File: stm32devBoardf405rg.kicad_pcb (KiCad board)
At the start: 4 copper layers, 0 parts

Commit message: assigned rough layout in pcb
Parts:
- added C1: 2u2, Capacitor_SMD:C_0603_1608Metric, F.Cu at (104.1, 142.2)
- added C10: 10n, Capacitor_SMD:C_0402_1005Metric, F.Cu at (165.6, 71.1)
- added C11: 12pF, Capacitor_SMD:C_0402_1005Metric, F.Cu at (68.1, 142.8)
- added C12: 12pF, Capacitor_SMD:C_0402_1005Metric, F.Cu at (68.1, 144.8)
- added C13: 47u, Capacitor_SMD:C_0603_1608Metric, F.Cu at (166.9, 129.5)
- added C14: 47u, Capacitor_SMD:C_0603_1608Metric, F.Cu at (164.3, 116.8)
- added C15: 47u, Capacitor_SMD:C_0603_1608Metric, F.Cu at (178.0, 114.2)
- added C16: 47u, Capacitor_SMD:C_0603_1608Metric, F.Cu at (178.0, 116.8)
- added C2: 2u2, Capacitor_SMD:C_0603_1608Metric, F.Cu at (104.1, 144.8)
- added C3: 4u7, Capacitor_SMD:C_0603_1608Metric, F.Cu at (98.3, 91.4)
- added C4: 100n, Capacitor_SMD:C_0402_1005Metric, F.Cu at (93.5, 87.5)
- added C5: 100n, Capacitor_SMD:C_0402_1005Metric, F.Cu at (93.5, 89.5)
- added C6: 100n, Capacitor_SMD:C_0402_1005Metric, F.Cu at (93.5, 91.4)
- added C7: 100n, Capacitor_SMD:C_0402_1005Metric, F.Cu at (96.4, 87.5)
- added C8: 100n, Capacitor_SMD:C_0402_1005Metric, F.Cu at (96.4, 89.5)
- added C9: 1u, Capacitor_SMD:C_0402_1005Metric, F.Cu at (165.1, 75.1)
- added D1: BLUE, LED_SMD:LED_0603_1608Metric, F.Cu at (151.6, 76.2)
- added D2: B5819W, Diode_SMD:D_SOD-123, F.Cu at (160.9, 134.6)
- added D3: RED, LED_SMD:LED_0603_1608Metric, F.Cu at (153.2, 99.1)
- added F1: 250mA, Fuse:Fuse_1206_3216Metric, F.Cu at (162.2, 141.3)
- added FB1: 600 @ 600MHz, Inductor_SMD:L_0805_2012Metric, F.Cu at (166.6, 134.6)
- added H1: MountingHole_Pad, MountingHole:MountingHole_4.3mm_M4_Pad_Via, F.Cu at (134.9, 93.7)
- added H2: MountingHole_Pad, MountingHole:MountingHole_4.3mm_M4_Pad_Via, F.Cu at (134.9, 103.9)
- added H3: MountingHole_Pad, MountingHole:MountingHole_4.3mm_M4_Pad_Via, F.Cu at (134.9, 114.0)
- added H4: MountingHole_Pad, MountingHole:MountingHole_4.3mm_M4_Pad_Via, F.Cu at (134.9, 124.2)
- added J1: Screw_Terminal_01x02, TerminalBlock_Phoenix:TerminalBlock_Phoenix_PT-1,5-2-3.5-H_1x02_P3.50mm_Horizontal, F.Cu at (142.7, 124.8)
- added J2: SWD, Connector_PinSocket_1.27mm:PinSocket_2x05_P1.27mm_Vertical_SMD, F.Cu at (117.6, 55.9)
- added J3: Conn_01x04, Connector_Molex:Molex_PicoBlade_53048-0410_1x04_P1.25mm_Horizontal, F.Cu at (96.5, 116.8)
- added J4: Conn_01x04, Connector_Molex:Molex_PicoBlade_53048-0410_1x04_P1.25mm_Horizontal, F.Cu at (94.0, 152.4)
- added J5: USB_B_Micro, Connector_USB:USB_Micro-B_Amphenol_10103594-0001LF_Horizontal, F.Cu at (115.7, 136.9)
- added L1: 3u3, Inductor_SMD:L_0805_2012Metric, F.Cu at (164.4, 78.7)
- added L2: 3u3, Inductor_SMD:L_0805_2012Metric, F.Cu at (176.7, 109.2)
- added Q1: AO3401A, Package_TO_SOT_SMD:SOT-23, F.Cu at (158.4, 128.6)
- added R1: 10k, Resistor_SMD:R_0402_1005Metric, F.Cu at (99.6, 71.1)
- added R10: 22, Resistor_SMD:R_0603_1608Metric, F.Cu at (125.3, 53.4)
- added R11: 22, Resistor_SMD:R_0603_1608Metric, F.Cu at (125.3, 55.9)
- added R12: 22, Resistor_SMD:R_0603_1608Metric, F.Cu at (125.3, 58.5)
- added R13: 22, Resistor_SMD:R_0603_1608Metric, F.Cu at (125.3, 61.0)
- added R14: 2k2, Resistor_SMD:R_0402_1005Metric, F.Cu at (104.7, 155.4)
- added R15: 2k2, Resistor_SMD:R_0402_1005Metric, F.Cu at (106.7, 155.4)
- added R16: 1K, Resistor_SMD:R_0603_1608Metric, F.Cu at (149.7, 100.0)
- added R2: 47, Resistor_SMD:R_0402_1005Metric, F.Cu at (68.1, 152.4)
- added R3: 1k5, Resistor_SMD:R_0603_1608Metric, F.Cu at (146.5, 76.2)
- added R4: 100K, Resistor_SMD:R_0603_1608Metric, F.Cu at (146.0, 92.4)
- added R5: 68K, Resistor_SMD:R_0603_1608Metric, F.Cu at (146.0, 94.9)
- added R6: 30K, Resistor_SMD:R_0603_1608Metric, F.Cu at (182.1, 109.2)
- added R7: 10k, Resistor_SMD:R_0603_1608Metric, F.Cu at (182.1, 111.7)
- added R8: 1K, Resistor_SMD:R_0603_1608Metric, F.Cu at (182.1, 114.2)
- added R9: 270, Resistor_SMD:R_0603_1608Metric, F.Cu at (182.1, 116.8)
- added SW1: SW_SPDT, Button_Switch_SMD:SW_SPDT_PCM12, F.Cu at (90.3, 64.4)
- added TPMP1: ~, Package_TO_SOT_SMD:SOT-23-6, F.Cu at (115.7, 146.4)
- added U1: STM32F405RGT6, Package_QFP:LQFP-64_10x10mm_P0.5mm, F.Cu at (94.6, 136.4)
- added U2: USBLC6-2SC6, Package_TO_SOT_SMD:SOT-23-6, F.Cu at (108.1, 137.2)
- added Y1: 16MZ, Crystal:Crystal_SMD_3225-4Pin_3.2x2.5mm, F.Cu at (62.4, 151.6)

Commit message: added pin no to TPMP2359 buck regulator
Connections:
- TPMP1 pad 1: (no net) -> BUCK_BS
- TPMP1 pad 2: (no net) -> GND
- TPMP1 pad 3: (no net) -> BUCK_FB
- TPMP1 pad 4: (no net) -> BUCK_EN
- TPMP1 pad 5: (no net) -> BUCK_IN
- TPMP1 pad 6: (no net) -> BUCK_SW
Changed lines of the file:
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@@
     (fp_line (start 0.8 1.45) (end -0.8 1.45)
       (stroke (width 0.1) (type solid)) (layer "F.Fab"))
-    (pad "1" smd roundrect (at -1.1375 -0.95) (size 1.325 0.6) (layers "F.Cu" "F.Paste" "F.Mask") (roundrect_rratio 0.25))
-    (pad "2" smd roundrect (at -1.1375 0) (size 1.325 0.6) (layers "F.Cu" "F.Paste" "F.Mask") (roundrect_rratio 0.25))
-    (pad "3" smd roundrect (at -1.1375 0.95) (size 1.325 0.6) (layers "F.Cu" "F.Paste" "F.Mask") (roundrect_rratio 0.25))
-    (pad "4" smd roundrect (at 1.1375 0.95) (size 1.325 0.6) (layers "F.Cu" "F.Paste" "F.Mask") (roundrect_rratio 0.25))
-    (pad "5" smd roundrect (at 1.1375 0) (size 1.325 0.6) (layers "F.Cu" "F.Paste" "F.Mask") (roundrect_rratio 0.25))
-    (pad "6" smd roundrect (at 1.1375 -0.95) (size 1.325 0.6) (layers "F.Cu" "F.Paste" "F.Mask") (roundrect_rratio 0.25))
+    (pad "1" smd roundrect (at -1.1375 -0.95) (size 1.325 0.6) (layers "F.Cu" "F.Paste" "F.Mask") (roundrect_rratio 0.25)
+      (net 10 "BUCK_BS") (pinfunction "BS") (pintype "input"))
+    (pad "2" smd roundrect (at -1.1375 0) (size 1.325 0.6) (layers "F.Cu" "F.Paste" "F.Mask") (roundrect_rratio 0.25)
+      (net 2 "GND") (pinfunction "GND") (pintype "input"))
+    (pad "3" smd roundrect (at -1.1375 0.95) (size 1.325 0.6) (layers "F.Cu" "F.Paste" "F.Mask") (roundrect_rratio 0.25)
+      (net 11 "BUCK_FB") (pinfunction "FB") (pintype "output"))
+    (pad "4" smd roundrect (at 1.1375 0.95) (size 1.325 0.6) (layers "F.Cu" "F.Paste" "F.Mask") (roundrect_rratio 0.25)
+      (net 36 "BUCK_EN") (pinfunction "EN") (pintype "input"))
+    (pad "5" smd roundrect (at 1.1375 0) (size 1.325 0.6) (layers "F.Cu" "F.Paste" "F.Mask") (roundrect_rratio 0.25)
+      (net 8 "BUCK_IN") (pinfunction "IN") (pintype "input"))
+    (pad "6" smd roundrect (at 1.1375 -0.95) (size 1.325 0.6) (layers "F.Cu" "F.Paste" "F.Mask") (roundrect_rratio 0.25)
+      (net 9 "BUCK_SW") (pinfunction "SW") (pintype "output"))
     (model "${KICAD6_3DMODEL_DIR}/Package_TO_SOT_SMD.3dshapes/SOT-23-6.wrl"
       (offset (xyz 0 0 0))

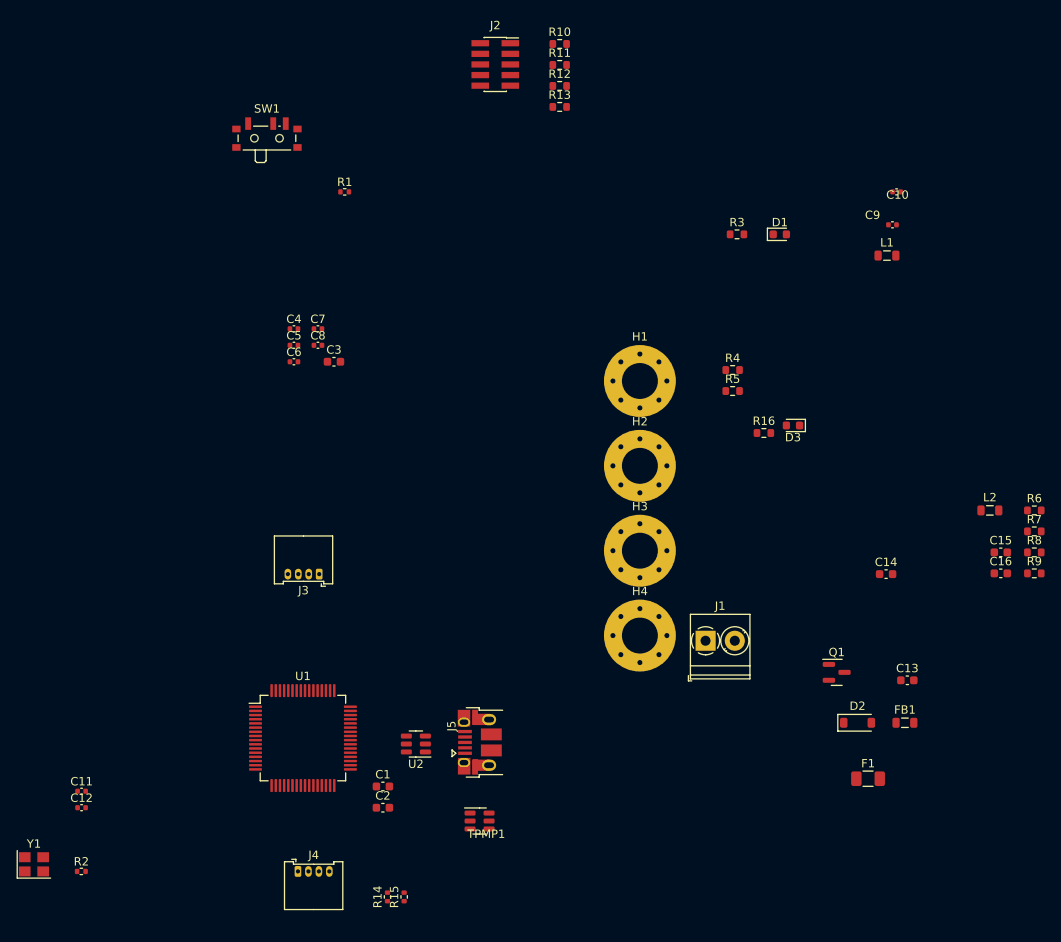
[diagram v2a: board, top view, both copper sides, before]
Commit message: fine placement for timer,indicator led,power decoupling capacitors,Boot pin
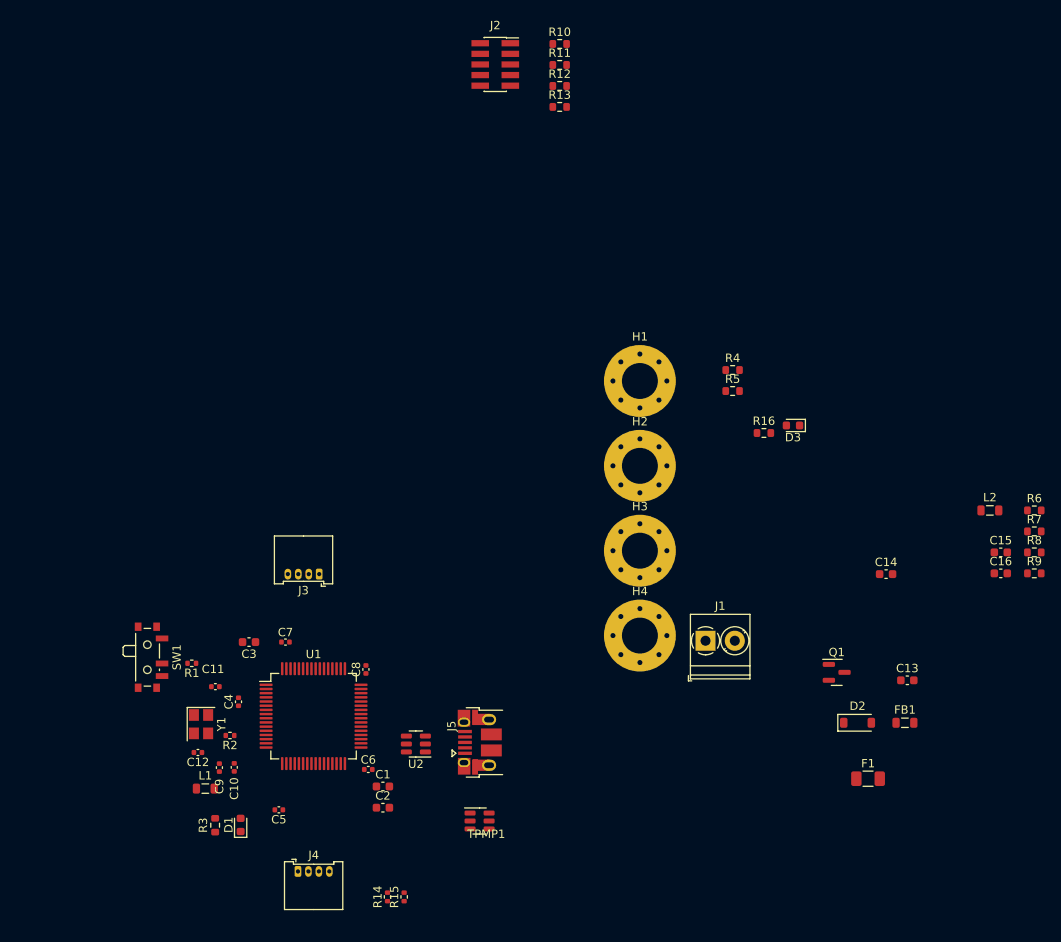
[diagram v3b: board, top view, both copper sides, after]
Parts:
- moved C10 104.9 mm to (86.4, 140.0), turned to 90 degrees
- moved L1 103.5 mm to (82.9, 142.5)
- moved C9 103.4 mm to (84.6, 140.0), turned to 90 degrees
- moved D1 95.6 mm to (87.1, 146.8), turned to 90 degrees
- moved R3 94.3 mm to (84.1, 146.9), turned to 90 degrees
- moved SW1 63.9 mm to (76.3, 126.8), turned to -90 degrees
- moved R1 59.3 mm to (81.3, 127.5), turned to 180 degrees
- moved C5 55.6 mm to (91.7, 145.0), turned to 180 degrees
- moved C6 49.6 mm to (102.4, 140.2)
- moved C4 45.1 mm to (86.9, 132.1), turned to 90 degrees
- moved C8 39.2 mm to (102.1, 128.2), turned to 90 degrees
- moved C7 37.7 mm to (92.5, 125.0)
- moved C3 35.0 mm to (88.1, 125.0), turned to 180 degrees
- moved Y1 26.1 mm to (82.4, 134.8), turned to -90 degrees
- moved R2 24.1 mm to (85.8, 136.1), turned to 180 degrees
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
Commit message: finished with the placing of component
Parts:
- moved R7 76.2 mm to (109.9, 136.1), turned to 180 degrees
- moved C15 74.7 mm to (106.4, 135.4)
- moved C16 74.7 mm to (106.4, 137.9)
- moved R6 74.7 mm to (110.2, 129.4)
- moved R8 74.1 mm to (109.9, 131.3), turned to 180 degrees
- moved R9 74.1 mm to (109.9, 133.9)
- moved L2 73.7 mm to (110.2, 140.9), turned to 90 degrees
- moved R10 69.8 mm to (113.3, 122.2), turned to -90 degrees
- moved H3 69.5 mm to (75.8, 150.6)
- moved R11 67.9 mm to (110.8, 122.2), turned to -90 degrees
- moved R12 66.0 mm to (108.3, 122.2), turned to -90 degrees
- moved R13 64.3 mm to (105.8, 122.2), turned to -90 degrees
- moved C14 60.8 mm to (110.2, 144.5), turned to -90 degrees
- moved H2 59.4 mm to (76.7, 115.8)
- moved J2 59.0 mm to (110.8, 114.5), turned to -90 degrees
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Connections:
- F1 pad 1: +12V -> Net-(D2-K)
- F1 pad 2: Net-(Q1-D) -> Net-(F1-Pad2)
- FB1 pad 2: Net-(D2-K) -> Net-(F1-Pad2)
- Q1 pad 3: Net-(Q1-D) -> +12V

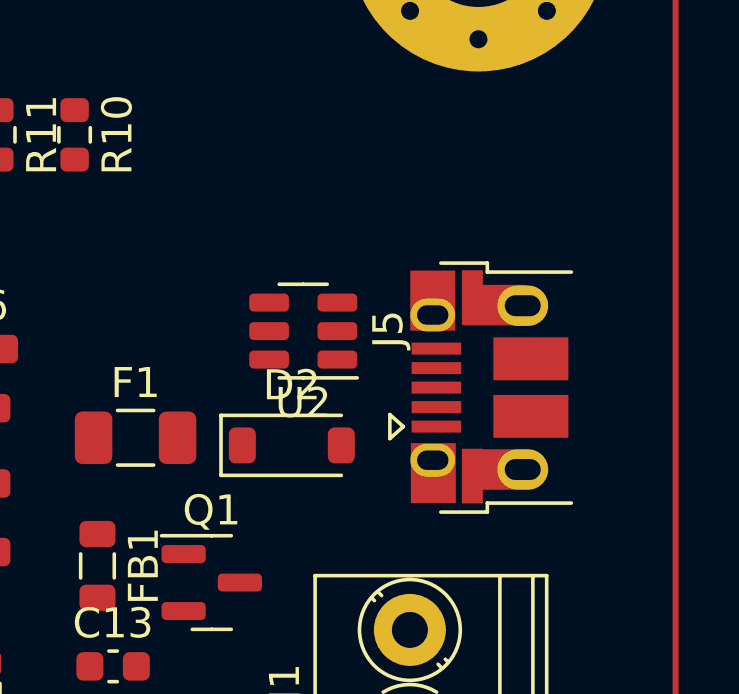
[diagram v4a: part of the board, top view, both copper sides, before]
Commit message: made GND and PWR cu layer
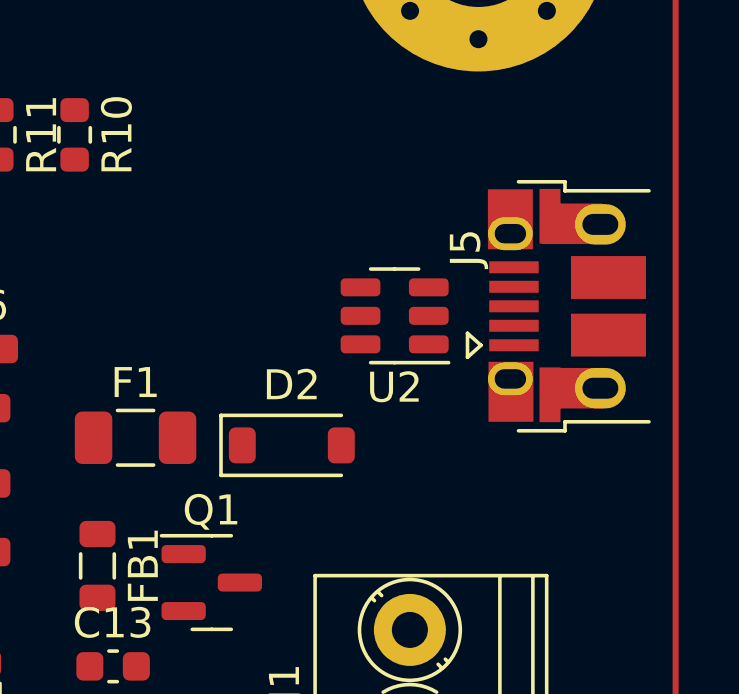
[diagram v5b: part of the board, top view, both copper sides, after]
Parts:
- moved J5 3.75 mm to (129.7, 127.9)
- moved U2 3.09 mm to (124.0, 128.3)
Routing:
- added copper zone on In1.Cu, net +3.3V
- added copper zone on In2.Cu, net +3.3V
- added copper zone on In1.Cu, net GND
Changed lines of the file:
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@@
   )
   (footprint "Connector_USB:USB_Micro-B_Amphenol_10103594-0001LF_Horizontal" (layer "F.Cu")
-    (at 127.107 130.637 90)
+    (at 129.695 127.927 90)
     (descr "Micro USB Type B 10103594-0001LF, http://cdn.amphenol-icc.com/media/wysiwyg/files/drawing/10103594.pdf")
     (tags "USB USB_B USB_micro USB_OTG")
@@
   )
   (footprint "Package_TO_SOT_SMD:SOT-23-6" (layer "F.Cu")
-    (at 120.904 128.778 180)
+    (at 123.952 128.27 180)
     (descr "SOT, 6 Pin (https://www.jedec.org/sites/default/files/docs/Mo-178c.PDF variant AB), generated with kicad-footprint-generator ipc_gullwing_generator.py")
     (tags "SOT TO_SOT_SMD")
@@
   (gr_arc (start 68.45589 117.245991) (mid 69.674158 111.286212) (end 74.603208 107.721437)
     (stroke (width 0.2) (type default)) (layer "F.Cu"))
+  (zone (net 2) (net_name "GND") (layer "In1.Cu") (hatch edge 0.5)
+    (connect_pads (clearance 0.5))
+    (min_thickness 0.25) (filled_areas_thickness no)
+    (fill yes (thermal_gap 0.5) (thermal_bridge_width 0.5))
+    (polygon
+      (pts
+        (xy 68.58 107.188)
+        (xy 133.604 107.696)
+        (xy 133.35 159.766)
+        (xy 68.072 159.004)
+      )
+    )
+  )
+  (zone (net 4) (net_name "+3.3V") (layers "In1.Cu" "In2.Cu") (hatch edge 0.5)
+    (connect_pads (clearance 0.5))
+    (min_thickness 0.25) (filled_areas_thickness no)
+    (fill yes (thermal_gap 0.5) (thermal_bridge_width 0.5))
+    (polygon
+      (pts
+        (xy 68.58 107.3069)
+        (xy 133.604 107.8149)
+        (xy 133.35 159.8849)
+        (xy 68.072 159.1229)
+      )
+    )
+  )
 )

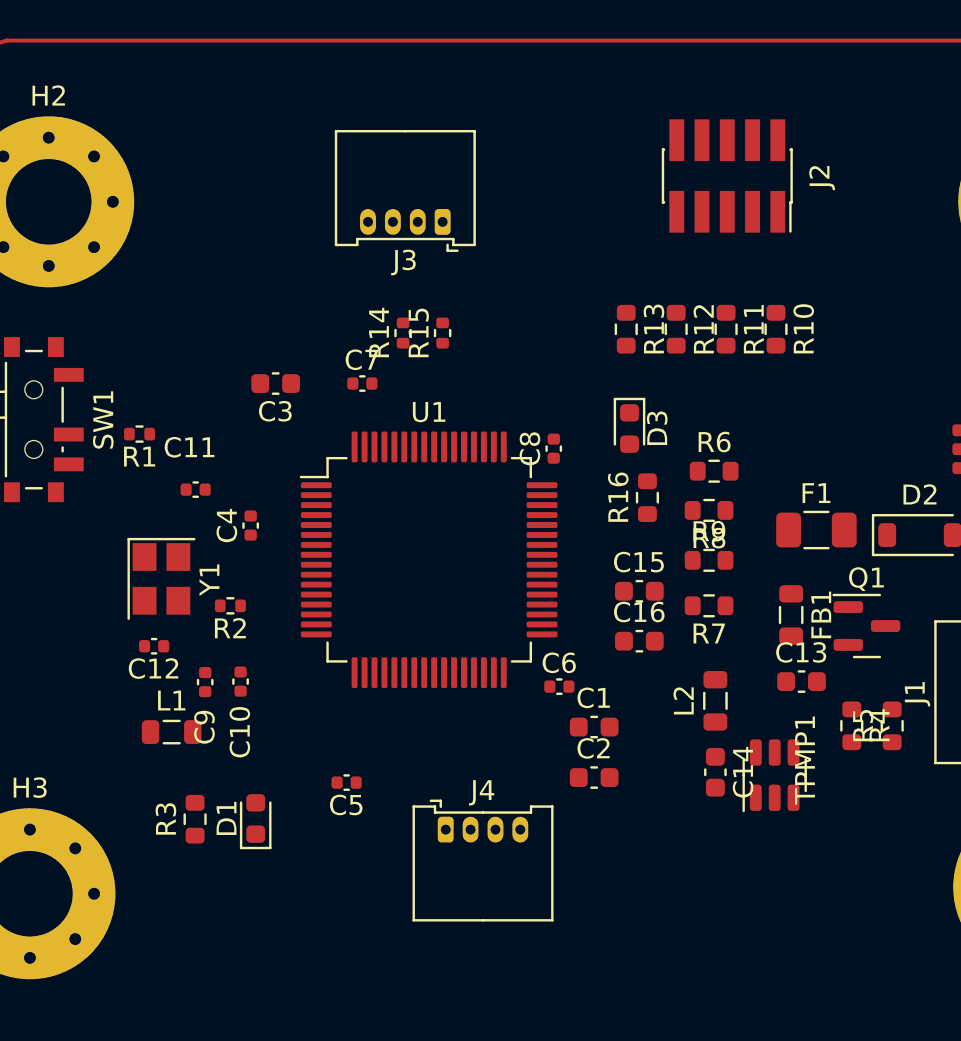
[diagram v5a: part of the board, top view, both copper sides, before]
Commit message: route decoupling capacitor,i2c,swd
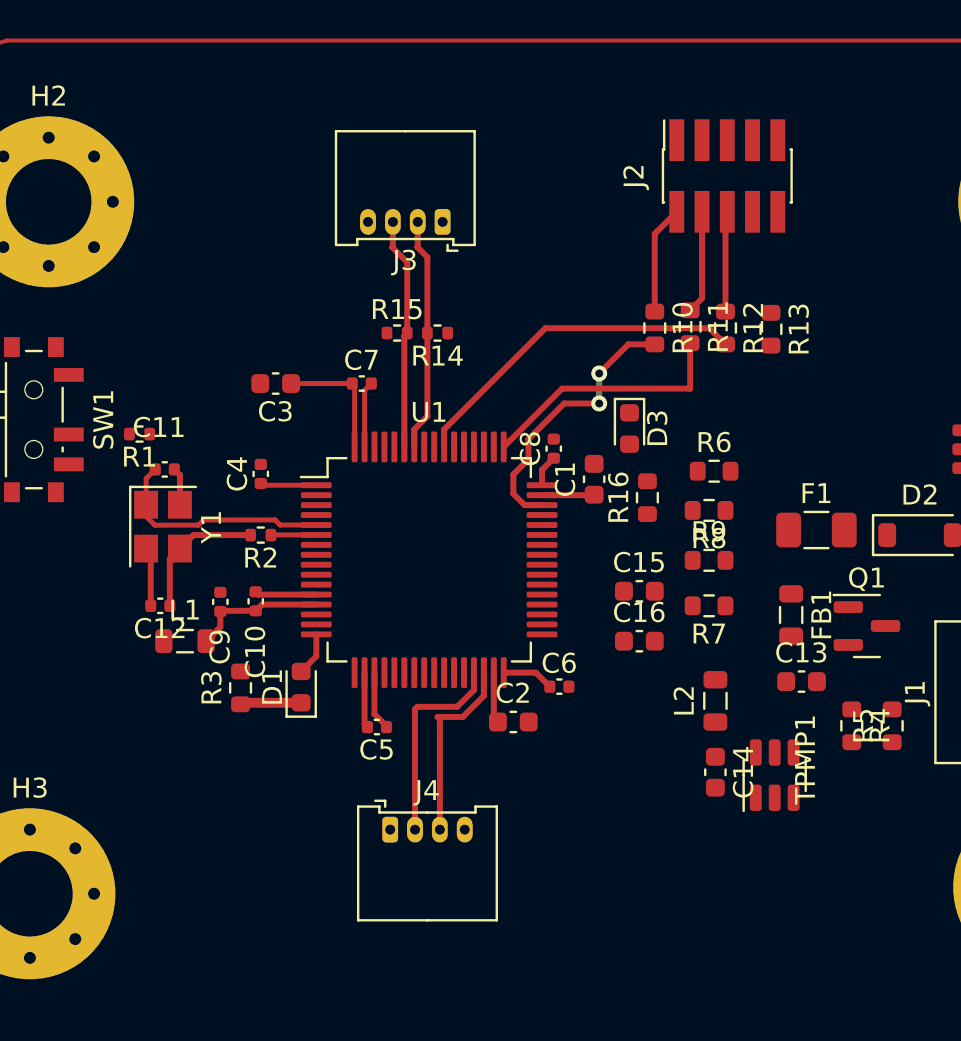
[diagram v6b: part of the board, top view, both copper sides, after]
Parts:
- moved C1 12.5 mm to (104.1, 129.8), turned to 90 degrees
- moved R13 7.28 mm to (113.0, 122.2)
- moved D1 6.99 mm to (89.4, 140.2)
- moved R3 6.99 mm to (86.4, 140.3)
- moved R10 6.10 mm to (107.2, 122.2)
- moved C2 4.93 mm to (100.1, 142.0)
- moved L1 4.62 mm to (83.6, 137.9)
- moved C10 4.11 mm to (87.1, 135.9)
- moved C9 4.11 mm to (85.3, 135.9)
- moved R2 3.87 mm to (87.4, 132.6)
- moved C5 3.18 mm to (93.2, 142.2)
- moved J4 2.79 mm to (93.9, 147.4)
- moved C4 2.65 mm to (87.4, 129.5)
- moved Y1 2.63 mm to (82.5, 132.2)
- moved R12 2.48 mm to (110.7, 122.2)
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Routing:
- net SWO: track 0.00 -> 17.5 mm
- net +3.3V: track 0.00 -> 16.3 mm
- net GND: track 0.00 -> 14.1 mm
- net SWDIO: track 0.00 -> 14.0 mm, vias 0 -> 2
- net SWCLK: track 0.00 -> 12.9 mm
- net I2C1_SDA: track 0.00 -> 12.0 mm
- net I2C1_SCL: track 0.00 -> 11.8 mm
- net HSE_IN: track 0.00 -> 11.5 mm
- net UART3_TX: track 0.00 -> 10.3 mm
- net UART3_RX: track 0.00 -> 9.65 mm
- net Net-(C12-Pad1): track 0.00 -> 6.92 mm
- net +3.3VA: track 0.00 -> 6.76 mm
- net Net-(J2-Pin_2): track 0.00 -> 5.48 mm
- net Net-(J2-Pin_4): track 0.00 -> 5.20 mm
- net Net-(J2-Pin_6): track 0.00 -> 5.05 mm
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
